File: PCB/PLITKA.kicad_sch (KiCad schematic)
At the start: 47 parts, among them SW1 SW_DPDT_x2, SW10 MX_SW_HS, SW11 MX_SW_HS, SW12 MX_SW_HS, SW13 MX_SW_HS, SW14 MX_SW_HS, SW15 MX_SW_HS, SW16 MX_SW_HS, SW17 MX_SW_HS, SW18 MX_SW_HS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

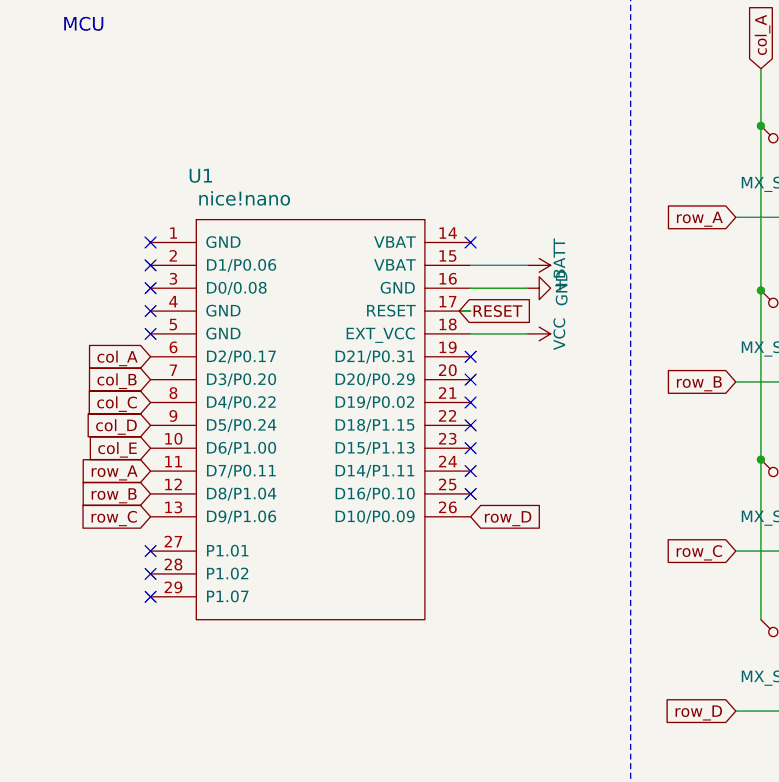
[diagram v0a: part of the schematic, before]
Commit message: Corrections to the symbol pads oredering and other definitions
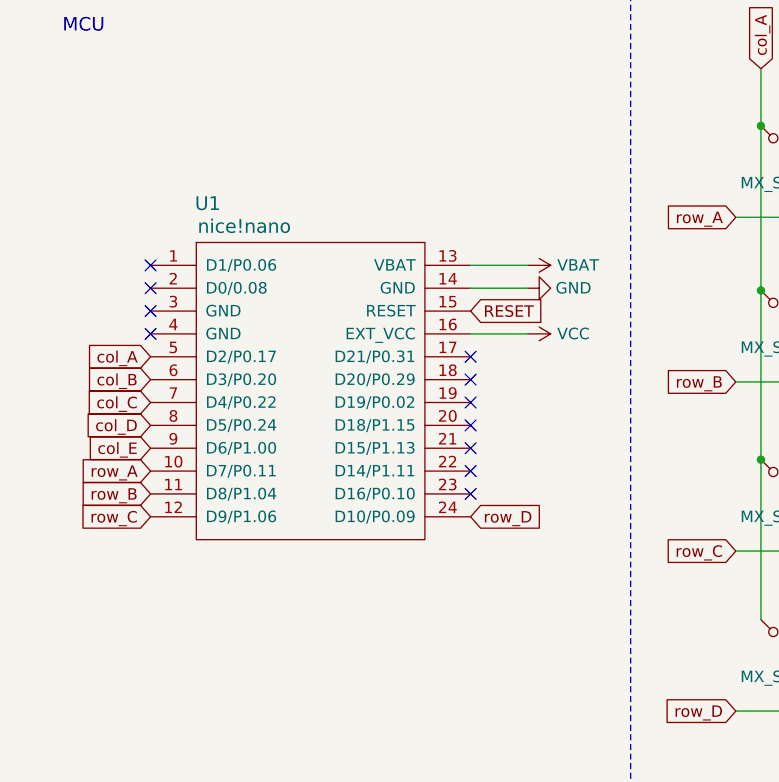
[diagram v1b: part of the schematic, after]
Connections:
- net +BATT: no longer U1.15 (VBAT)
- net GND: now also U1.14 (GND); no longer U1.16 (GND)
- net RESET: now also U1.15 (RESET); no longer U1.17 (RESET)
- net VCC: now also U1.16 (EXT_VCC); no longer U1.18 (EXT_VCC)
- net col_A: now also U1.5 (D2/P0.17); no longer U1.6 (D2/P0.17)
- net col_B: now also U1.6 (D3/P0.20); no longer U1.7 (D3/P0.20)
- net col_C: now also U1.7 (D4/P0.22); no longer U1.8 (D4/P0.22)
- net col_D: now also U1.8 (D5/P0.24); no longer U1.9 (D5/P0.24)
- net col_E: now also U1.9 (D6/P1.00); no longer U1.10 (D6/P1.00)
- net row_A: now also U1.10 (D7/P0.11); no longer U1.11 (D7/P0.11)
- net row_B: now also U1.11 (D8/P1.04); no longer U1.12 (D8/P1.04)
- net row_C: now also U1.12 (D9/P1.06); no longer U1.13 (D9/P1.06)
- net row_D: now also U1.24 (D10/P0.09); no longer U1.26 (D10/P0.09)
- new net VBAT: U1.13 (VBAT)
- no-connect marks 17 -> 12
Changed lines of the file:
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@@
 	)
 	(no_connect
-		(at 26.67 82.55)
-	)
-	(no_connect
 		(at 66.294 117.602)
 	)
 	(no_connect
-		(at 26.67 80.01)
-	)
-	(no_connect
 		(at 62.23 60.96)
 	)
@@
 	)
 	(no_connect
-		(at 26.67 43.18)
-	)
-	(no_connect
-		(at 62.23 43.18)
-	)
-	(no_connect
 		(at 26.67 53.34)
 	)
@@
 		(at 26.67 48.26)
 	)
-	(no_connect
-		(at 26.67 77.47)
-	)
 	(wire
 		(pts
@@
 		)
 	)
-	(wire
-		(pts
-			(xy 60.96 50.8) (xy 62.23 50.8)
-		)
-		(stroke
-			(width 0)
-			(type default)
-		)
-	)
 	(label "PAD2"
 		(at 34.29 123.952 0)
@@
 	(global_label "RESET"
 		(shape input)
-		(at 60.96 50.8 0)
+		(at 62.23 50.8 0)
 		(fields_autoplaced yes)
 		(effects
@@
 		)
 		(property "Intersheetrefs" "${INTERSHEET_REFS}"
-			(at 69.1183 50.7206 0)
+			(at 70.3883 50.7206 0)
 			(hide yes)
 			(show_name no)
@@
 		)
 		(property "Value" "VCC"
-			(at 72.136 53.34 0)
+			(at 73.66 53.34 90)
 			(show_name no)
 			(do_not_autoplace no)
@@
 			)
 		)
-		(property "Value" "+BATT"
-			(at 72.136 45.72 0)
+		(property "Value" "VBAT"
+			(at 74.168 45.72 90)
 			(show_name no)
 			(do_not_autoplace no)
@@
 		)
 		(property "Value" "GND"
-			(at 72.39 48.26 0)
+			(at 73.66 48.26 90)
 			(show_name no)
 			(do_not_autoplace no)
@@
 		(dnp no)
 		(property "Reference" "U1"
-			(at 32.258 35.814 0)
+			(at 33.02 38.862 0)
 			(show_name no)
 			(do_not_autoplace no)
@@
 		)
 		(property "Value" "nice!nano"
-			(at 37.084 38.354 0)
+			(at 37.084 41.402 0)
 			(show_name no)
 			(do_not_autoplace no)
@@
 		)
 		(property "Footprint" "PLITKA:nice_nano"
-			(at 43.942 88.138 0)
+			(at 44.704 80.01 0)
 			(hide yes)
 			(show_name no)
@@
 			)
 		)
-		(pin "1"
-		)
 		(pin "10"
 		)
@@
 		(pin "23"
 		)
-		(pin "14"
-		)
-		(pin "26"
+		(pin "1"
 		)
-		(pin "25"
+		(pin "13"
 		)
 		(pin "17"
@@
 		(pin "9"
 		)
-		(pin "13"
+		(pin "14"
 		)
 		(pin "16"
 		)
-		(pin "28"
-		)
-		(pin "29"
-		)
-		(pin "27"
-		)
 		(instances

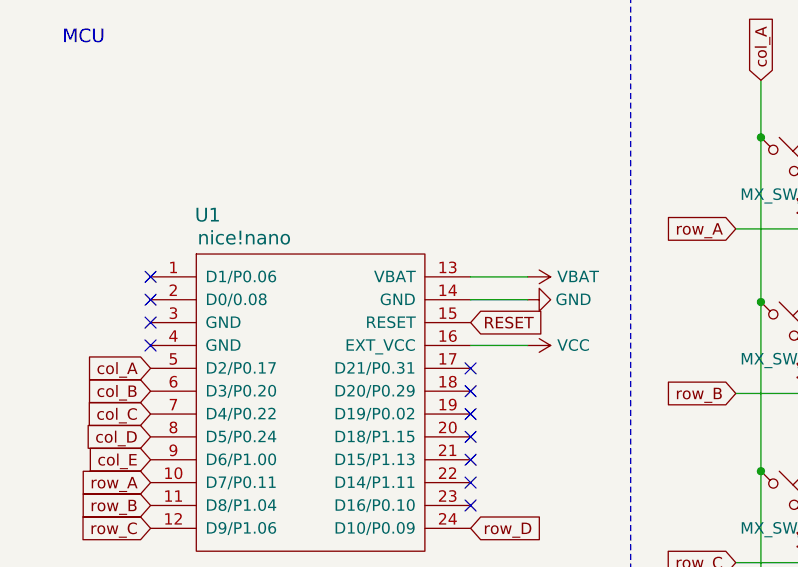
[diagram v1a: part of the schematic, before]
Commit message: Corrected the references to the footprints
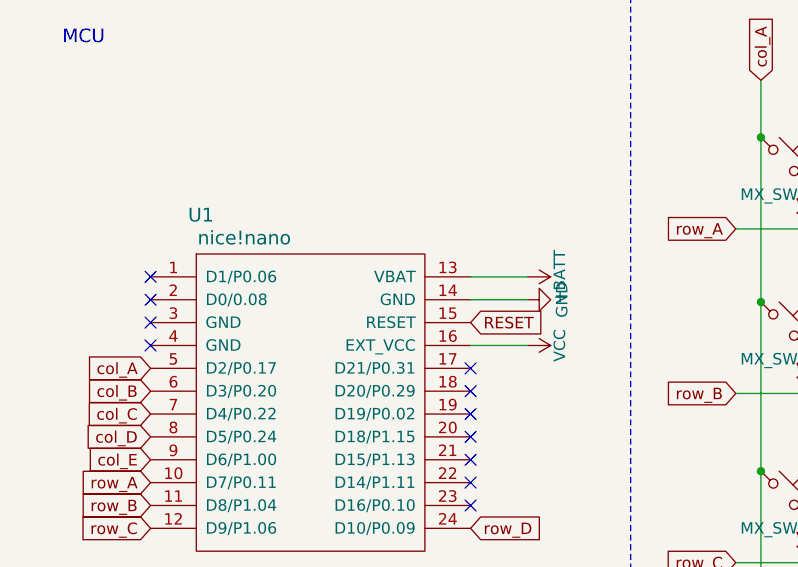
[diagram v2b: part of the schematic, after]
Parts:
- SW10, SW11, SW12, SW13, SW14, SW15, SW16, SW17, SW18, SW2, SW3, SW4, SW5, SW6, SW7, SW8, SW9: footprint marbastlib-mx:SW_MX_HS_1u -> PLITKA:Kailh_socket_PG1350_optional_reversible
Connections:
- net VBAT is gone; now on net +BATT: U1.13 (VBAT)
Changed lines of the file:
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@@
 			)
 		)
-		(property "Footprint" "marbastlib-mx:SW_MX_HS_1u"
+		(property "Footprint" "PLITKA:Kailh_socket_PG1350_optional_reversible"
 			(at 118.872 51.054 0)
 			(hide yes)
@@
 			)
 		)
-		(property "Footprint" "marbastlib-mx:SW_MX_HS_1u"
+		(property "Footprint" "PLITKA:Kailh_socket_PG1350_optional_reversible"
 			(at 140.716 32.766 0)
 			(hide yes)
@@
 			)
 		)
-		(property "Footprint" "marbastlib-mx:SW_MX_HS_1u"
+		(property "Footprint" "PLITKA:Kailh_socket_PG1350_optional_reversible"
 			(at 129.794 51.054 0)
 			(hide yes)
@@
 			)
 		)
-		(property "Footprint" "marbastlib-mx:SW_MX_HS_1u"
+		(property "Footprint" "PLITKA:Kailh_socket_PG1350_optional_reversible"
 			(at 118.872 32.766 0)
 			(hide yes)
@@
 			)
 		)
-		(property "Footprint" "marbastlib-mx:SW_MX_HS_1u"
+		(property "Footprint" "PLITKA:Kailh_socket_PG1350_optional_reversible"
 			(at 118.872 69.85 0)
 			(hide yes)
@@
 		)
 		(property "Value" "VCC"
-			(at 73.66 53.34 90)
+			(at 72.136 53.34 0)
 			(show_name no)
 			(do_not_autoplace no)
@@
 			)
 		)
-		(property "Footprint" "marbastlib-mx:SW_MX_HS_1u"
+		(property "Footprint" "PLITKA:Kailh_socket_PG1350_optional_reversible"
 			(at 97.028 87.63 0)
 			(hide yes)
@@
 			)
 		)
-		(property "Footprint" "marbastlib-mx:SW_MX_HS_1u"
+		(property "Footprint" "PLITKA:Kailh_socket_PG1350_optional_reversible"
 			(at 129.794 32.766 0)
 			(hide yes)
@@
 			)
 		)
-		(property "Value" "VBAT"
-			(at 74.168 45.72 90)
+		(property "Value" "+BATT"
+			(at 72.136 45.72 0)
 			(show_name no)
 			(do_not_autoplace no)
@@
 			)
 		)
-		(property "Footprint" "marbastlib-mx:SW_MX_HS_1u"
+		(property "Footprint" "PLITKA:Kailh_socket_PG1350_optional_reversible"
 			(at 107.95 69.85 0)
 			(hide yes)
@@
 			)
 		)
-		(property "Footprint" "marbastlib-mx:SW_MX_HS_1u"
+		(property "Footprint" "PLITKA:Kailh_socket_PG1350_optional_reversible"
 			(at 97.028 32.766 0)
 			(hide yes)
@@
 			)
 		)
-		(property "Footprint" "marbastlib-mx:SW_MX_HS_1u"
+		(property "Footprint" "PLITKA:Kailh_socket_PG1350_optional_reversible"
 			(at 140.716 51.054 0)
 			(hide yes)
@@
 			)
 		)
-		(property "Footprint" "marbastlib-mx:SW_MX_HS_1u"
+		(property "Footprint" "PLITKA:Kailh_socket_PG1350_optional_reversible"
 			(at 140.716 69.85 0)
 			(hide yes)
@@
 			)
 		)
-		(property "Footprint" "marbastlib-mx:SW_MX_HS_1u"
+		(property "Footprint" "PLITKA:Kailh_socket_PG1350_optional_reversible"
 			(at 97.028 69.85 0)
 			(hide yes)
@@
 			)
 		)
-		(property "Footprint" "marbastlib-mx:SW_MX_HS_1u"
+		(property "Footprint" "PLITKA:Kailh_socket_PG1350_optional_reversible"
 			(at 107.95 87.63 0)
 			(hide yes)
@@
 			)
 		)
-		(property "Footprint" "marbastlib-mx:SW_MX_HS_1u"
+		(property "Footprint" "PLITKA:Kailh_socket_PG1350_optional_reversible"
 			(at 107.95 51.054 0)
 			(hide yes)
@@
 		)
 		(property "Value" "GND"
-			(at 73.66 48.26 90)
+			(at 72.39 48.26 0)
 			(show_name no)
 			(do_not_autoplace no)
@@
 			)
 		)
-		(property "Footprint" "marbastlib-mx:SW_MX_HS_1u"
+		(property "Footprint" "PLITKA:Kailh_socket_PG1350_optional_reversible"
 			(at 129.794 69.85 0)
 			(hide yes)
@@
 		(dnp no)
 		(property "Reference" "U1"
-			(at 33.02 38.862 0)
+			(at 32.258 38.862 0)
 			(show_name no)
 			(do_not_autoplace no)
@@
 			)
 		)
-		(property "Footprint" "marbastlib-mx:SW_MX_HS_1u"
+		(property "Footprint" "PLITKA:Kailh_socket_PG1350_optional_reversible"
 			(at 107.95 32.766 0)
 			(hide yes)
@@
 			)
 		)
-		(property "Footprint" "marbastlib-mx:SW_MX_HS_1u"
+		(property "Footprint" "PLITKA:Kailh_socket_PG1350_optional_reversible"
 			(at 97.028 51.054 0)
 			(hide yes)
